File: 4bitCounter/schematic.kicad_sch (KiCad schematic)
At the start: 19 parts, among them Q1 PN2222A, U1 NE555P, U3 74LS161

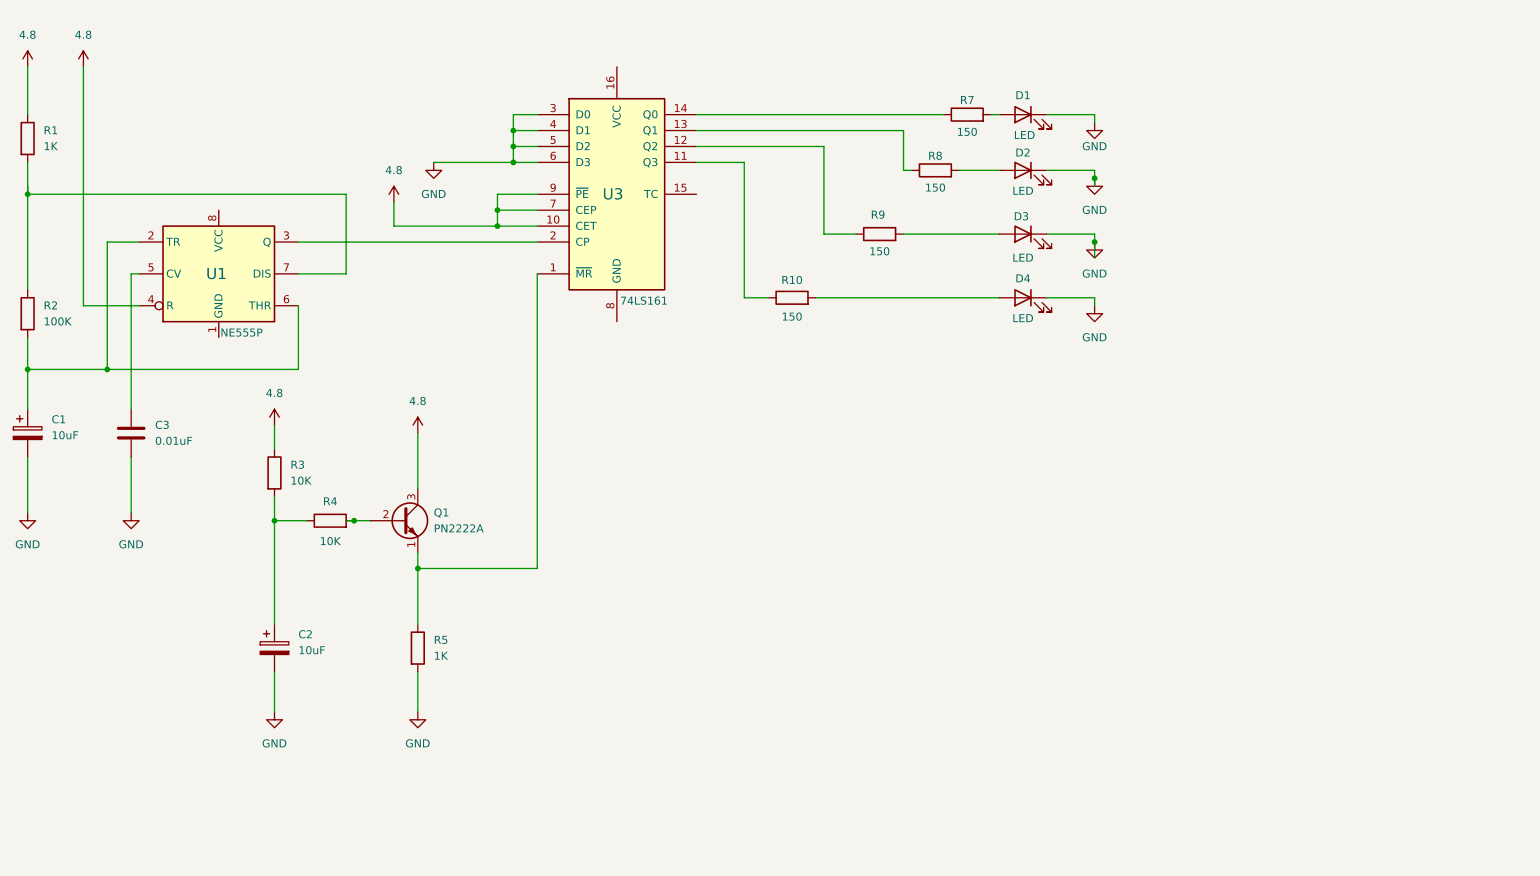
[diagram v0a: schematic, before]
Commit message: Updates on footprints and schematic
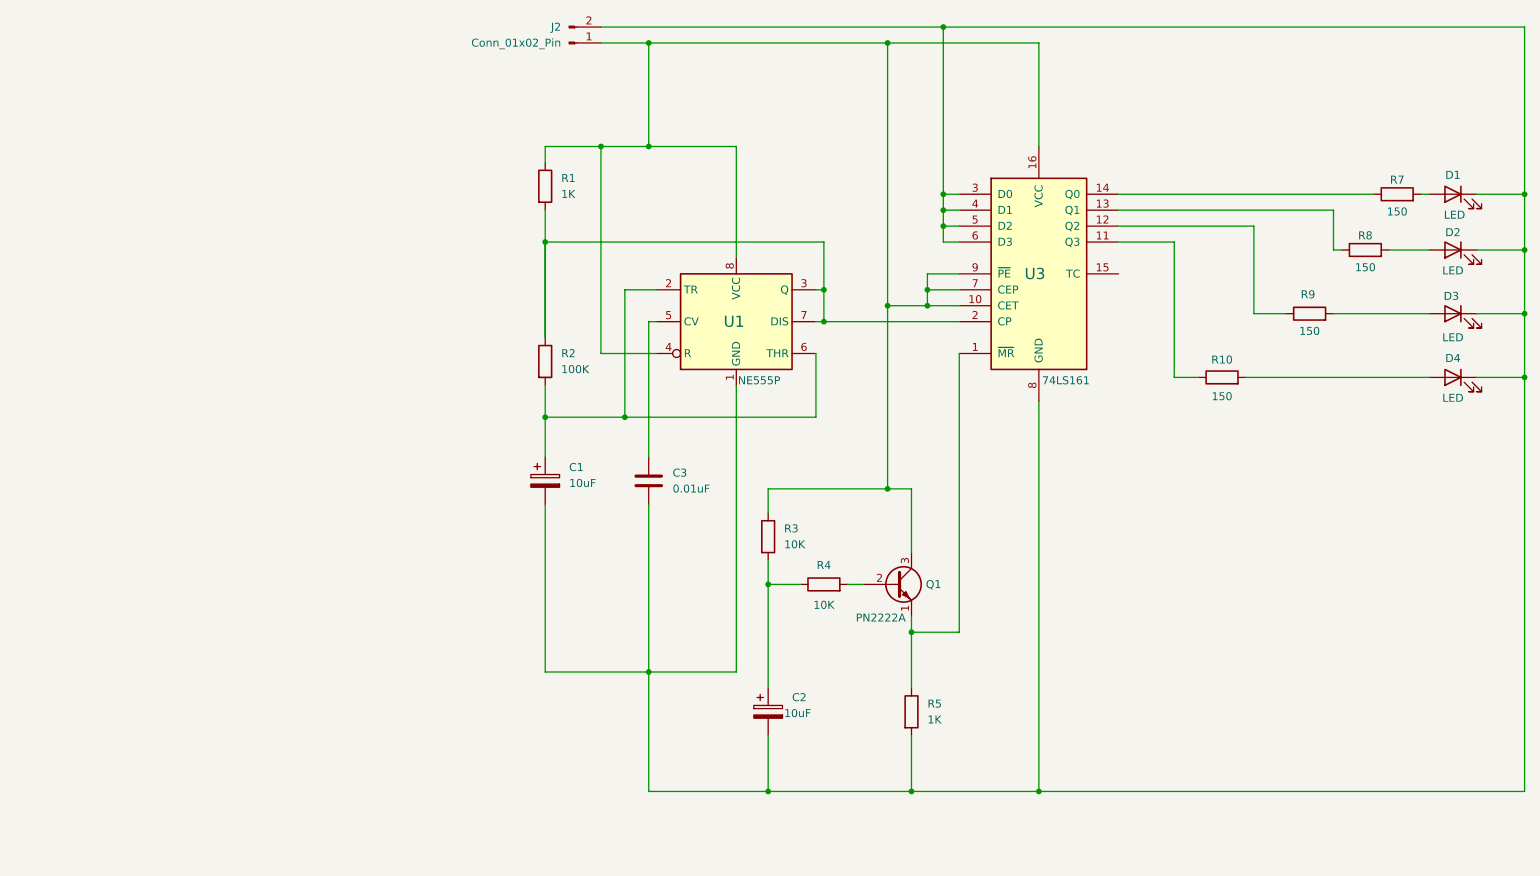
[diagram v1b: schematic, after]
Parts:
- added J2: Conn_01x02_Pin, CounterProject:Connector, symbol Connector:Conn_01x02_Pin
- C1, C2: footprint Capacitor_THT:CP_Radial_D4.0mm_P2.00mm -> CounterProject:Capacitor
- C3: footprint Capacitor_THT:CP_Radial_D5.0mm_P2.00mm -> CounterProject:Capacitor
- D1, D2, D3, D4: footprint LED_THT:LED_D5.0mm_Horizontal_O6.35mm_Z9.0mm -> CounterProject:LED
- Q1: footprint Package_TO_SOT_THT:TO-92_Inline -> CounterProject:transistor
- R1, R10, R2, R3, R5, R7, R8, R9: footprint Resistor_THT:R_Axial_DIN0922_L20.0mm_D9.0mm_P30.48mm_Horizontal -> CounterProject:Resistor
- R4: footprint Resistor_THT:R_Axial_DIN0922_L20.0mm_D9.0mm_P30.48mm_Horizontal -> 4bitCounter:Resistor
- U1: footprint Package_DIP:DIP-8_W7.62mm -> CounterProject:Timer
- U3: footprint Package_DIP:DIP-16_W7.62mm -> CounterProject:CounterChip
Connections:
- net 4.8 is gone; now on an unnamed net: Q1.3 (C), R1.1, R3.1, U1.4 (R), U3.10 (CET), U3.7 (CEP), U3.9 (~{PE})
- net GND is gone; now on an unnamed net: C1.2, C2.2, C3.2, D1.1 (K), D2.1 (K), D3.1 (K), D4.1 (K), R5.2, U3.3 (D0), U3.4 (D1), U3.5 (D2), U3.6 (D3)
- net at R1.2, R2.1, U1.7 (DIS): now also U1.3 (Q), U3.2 (CP)
- net at U1.1 (GND): now also U3.8 (GND), J2.2 (Pin_2)
- net at U1.8 (VCC): now also U3.16 (VCC), J2.1 (Pin_1)
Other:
- moved on the sheet: C1, C2, C3, D1, D2, D3, D4, Q1, R1, R10, R2, R3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

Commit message: Update footprints and pcb
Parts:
- Q1: footprint CounterProject:transistor -> CounterProject:Transistor
- R4: footprint 4bitCounter:Resistor -> CounterProject:Resistor
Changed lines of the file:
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@@
 			)
 		)
-		(property "Footprint" "4bitCounter:Resistor"
+		(property "Footprint" "CounterProject:Resistor"
 			(at 165.1 127.508 90)
 			(effects
@@
 			)
 		)
-		(property "Footprint" "CounterProject:transistor"
+		(property "Footprint" "CounterProject:Transistor"
 			(at 181.61 127.635 0)
 			(effects
@@
 					(size 1.27 1.27)
 				)
-				(hide yes)
-			)
-		)
+			)
+		)

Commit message: update pcb and schematic
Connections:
- net GND: now reaches C1.2, C2.2, C3.2, D1.1 (K), D2.1 (K), D3.1 (K), D4.1 (K), J2.2 (Pin_2), R5.2, U1.1 (GND), U3.3 (D0), U3.4 (D1), U3.5 (D2), U3.6 (D3), U3.8 (GND)
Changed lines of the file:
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@@
+	)
+	(junction
+		(at 163.83 158.75)
+		(diameter 0)
+		(color 0 0 0 0)
 	)
 	(junction
@@
 		(pts
 			(xy 133.35 78.74) (xy 133.35 99.06)
+		)
+		(stroke
+			(width 0)
+			(type default)
+		)
+	)
+	(wire
+		(pts
+			(xy 163.83 158.75) (xy 163.83 163.83)
 		)
 		(stroke
@@
 	(wire
 		(pts
-			(xy 156.21 158.75) (xy 179.07 158.75)
+			(xy 156.21 158.75) (xy 163.83 158.75)
 		)
 		(stroke
@@
 		(pts
 			(xy 246.38 82.55) (xy 261.62 82.55)
+		)
+		(stroke
+			(width 0)
+			(type default)
+		)
+	)
+	(wire
+		(pts
+			(xy 163.83 158.75) (xy 179.07 158.75)
 		)
 		(stroke
@@
 	)
 	(symbol
+		(lib_id "power:GND")
+		(at 163.83 163.83 0)
+		(unit 1)
+		(exclude_from_sim no)
+		(in_bom yes)
+		(on_board yes)
+		(dnp no)
+		(fields_autoplaced yes)
+		(property "Reference" "#PWR01"
+			(at 163.83 170.18 0)
+			(effects
+				(font
+					(size 1.27 1.27)
+				)
+				(hide yes)
+			)
+		)
+		(property "Value" "GND"
+			(at 163.83 168.91 0)
+			(effects
+				(font
+					(size 1.27 1.27)
+				)
+			)
+		)
+		(property "Footprint" ""
+			(at 163.83 163.83 0)
+			(effects
+				(font
+					(size 1.27 1.27)
+				)
+				(hide yes)
+			)
+		)
+		(property "Datasheet" ""
+			(at 163.83 163.83 0)
+			(effects
+				(font
+					(size 1.27 1.27)
+				)
+				(hide yes)
+			)
+		)
+		(property "Description" "Power symbol creates a global label with name \"GND\" , ground"
+			(at 163.83 163.83 0)
+			(effects
+				(font
+					(size 1.27 1.27)
+				)
+				(hide yes)
+			)
+		)
+		(pin "1"
+		)
+		(instances
+			(project ""
+				(path "/04b70f03-7b1f-4ee7-81cc-b757f4d3e55c"
+					(reference "#PWR01")
+					(unit 1)
+				)
+			)
+		)
+	)
+	(symbol
 		(lib_id "Timer:NE555P")
 		(at 151.13 83.82 0)
@@
 					(size 1.27 1.27)
 				)
-			)
-		)
+				(hide yes)
+			)
+		)
